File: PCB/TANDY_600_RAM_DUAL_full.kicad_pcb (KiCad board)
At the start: 2 copper layers, 74.9 x 21.6 mm, 7 parts, among them CN1 TANDY_600_RAM_BUS, CN2 TANDY_600_RAM_BUS, U1 AS6C4008, U2 74HC148, U3 74LVC1G02

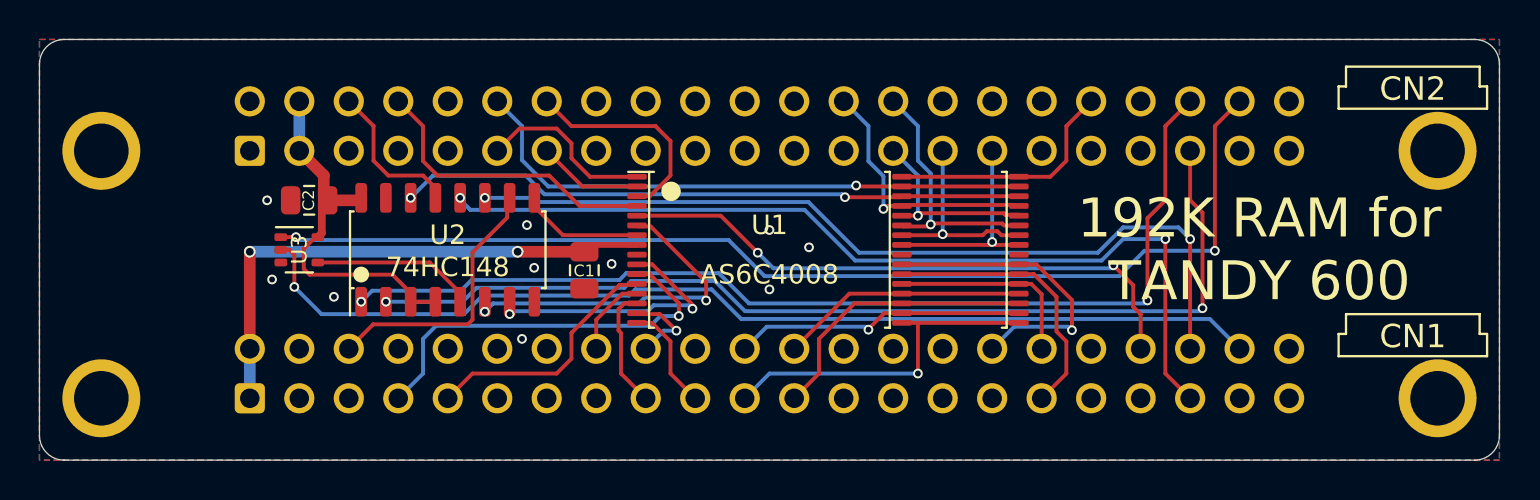
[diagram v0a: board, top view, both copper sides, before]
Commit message: footprints, ground paths
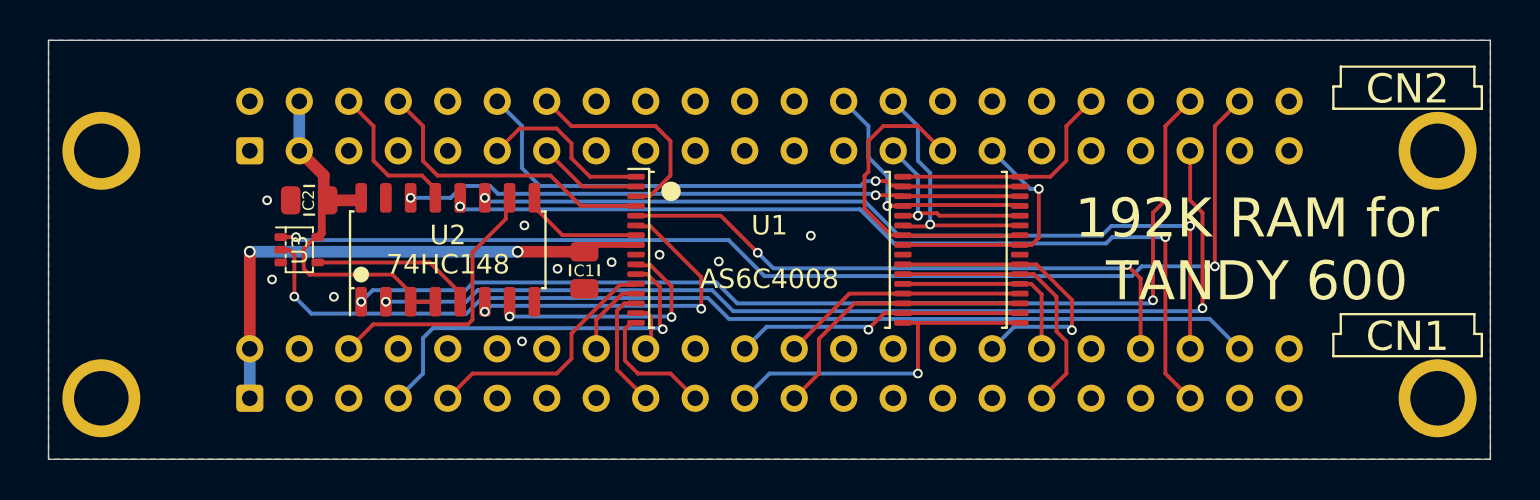
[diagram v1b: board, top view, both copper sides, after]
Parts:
- CN1, CN2: footprint 000_LOCAL:DIN41612-2x22_male_vertical -> 000_LOCAL:DIN-41612_02x22_male_vertical
- turned CN1 to 180 degrees
- turned CN2 to 180 degrees
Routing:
- net /D4: track 10.5 -> 16.8 mm, vias 1 -> 0
- net /D3: track 10.8 -> 12.8 mm
- net /A5: track 4.36 -> 2.60 mm, vias 1 -> 0
- net /A16: track 14.2 -> 12.9 mm
- net /A4: track 5.56 -> 6.73 mm
- net /~{B1_CS1_C}: track 46.7 -> 45.9 mm
- net /A14: track 20.6 -> 19.9 mm
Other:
- board size 74.9 x 21.6 mm -> 74 x 21.5 mm
